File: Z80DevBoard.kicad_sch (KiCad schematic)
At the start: 170 parts, among them J1 Conn_01x02_Pin, J2 Conn_02x20_Top_Bottom, J3 Conn_02x10_Top_Bottom, SW1 WAIT, SW2 RESET, SW3 Z80BOOT, SW4 RPBOOT, SW5 SW_Nidec_CAS-120A1, SW6 Z80_CLOCK, U1 74HC14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

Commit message: Fixed the size of the footprint of the fuse.
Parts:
- F1: footprint Fuse:Fuse_0402_1005Metric -> Fuse:Fuse_0603_1608Metric
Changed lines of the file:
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@@
 	(title_block
 		(title "Z80DevBoard")
-		(date "2026-03-26")
+		(date "2026-03-30")
 		(company "Gianluca Rainis")
 		(comment 1 "gianluca-rainis on GitHub")
@@
 			)
 		)
-		(property "Footprint" "Fuse:Fuse_0402_1005Metric"
+		(property "Footprint" "Fuse:Fuse_0603_1608Metric"
 			(at 22.098 40.64 90)
 			(effects

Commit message: Made a custom footprint for the switch.
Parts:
- SW5: footprint Button_Switch_THT:SW_Slide_SPDT_Straight_CK_OS102011MS2Q -> customFootprints:SW_Slide-03_Wuerth-WS-SLTV
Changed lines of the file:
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@@
 			)
 		)
-		(property "Footprint" "Button_Switch_THT:SW_Slide_SPDT_Straight_CK_OS102011MS2Q"
+		(property "Footprint" "customFootprints:SW_Slide-03_Wuerth-WS-SLTV"
 			(at 128.27 55.88 0)
 			(effects

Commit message: Fixed the size of the capacitors.
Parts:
- C1, C10, C11, C12, C13, C14, C2, C3, C4, C5, C6, C7, C8, C9: footprint Capacitor_THT:CP_Radial_D4.0mm_P2.00mm -> Capacitor_THT:CP_Radial_D5.0mm_P2.50mm
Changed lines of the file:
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@@
 	(title_block
 		(title "Z80DevBoard")
-		(date "2026-03-30")
+		(date "2026-03-31")
 		(company "Gianluca Rainis")
 		(comment 1 "gianluca-rainis on GitHub")
@@
 			)
 		)
-		(property "Footprint" "Capacitor_THT:CP_Radial_D4.0mm_P2.00mm"
+		(property "Footprint" "Capacitor_THT:CP_Radial_D5.0mm_P2.50mm"
 			(at 221.2848 287.02 0)
 			(effects
@@
 			)
 		)
-		(property "Footprint" "Capacitor_THT:CP_Radial_D4.0mm_P2.00mm"
+		(property "Footprint" "Capacitor_THT:CP_Radial_D5.0mm_P2.50mm"
 			(at 110.7948 25.4 0)
 			(effects
@@
 			)
 		)
-		(property "Footprint" "Capacitor_THT:CP_Radial_D4.0mm_P2.00mm"
+		(property "Footprint" "Capacitor_THT:CP_Radial_D5.0mm_P2.50mm"
 			(at 20.6248 72.39 0)
 			(effects
@@
 			)
 		)
-		(property "Footprint" "Capacitor_THT:CP_Radial_D4.0mm_P2.00mm"
+		(property "Footprint" "Capacitor_THT:CP_Radial_D5.0mm_P2.50mm"
 			(at 43.4848 31.75 0)
 			(effects
@@
 			)
 		)
-		(property "Footprint" "Capacitor_THT:CP_Radial_D4.0mm_P2.00mm"
+		(property "Footprint" "Capacitor_THT:CP_Radial_D5.0mm_P2.50mm"
 			(at 80.3148 261.62 0)
 			(effects
@@
 			)
 		)
-		(property "Footprint" "Capacitor_THT:CP_Radial_D4.0mm_P2.00mm"
+		(property "Footprint" "Capacitor_THT:CP_Radial_D5.0mm_P2.50mm"
 			(at 71.4248 72.39 0)
 			(effects
@@
 			)
 		)
-		(property "Footprint" "Capacitor_THT:CP_Radial_D4.0mm_P2.00mm"
+		(property "Footprint" "Capacitor_THT:CP_Radial_D5.0mm_P2.50mm"
 			(at 66.3448 31.75 0)
 			(effects
@@
 			)
 		)
-		(property "Footprint" "Capacitor_THT:CP_Radial_D4.0mm_P2.00mm"
+		(property "Footprint" "Capacitor_THT:CP_Radial_D5.0mm_P2.50mm"
 			(at 218.7448 322.58 0)
 			(effects
@@
 			)
 		)
-		(property "Footprint" "Capacitor_THT:CP_Radial_D4.0mm_P2.00mm"
+		(property "Footprint" "Capacitor_THT:CP_Radial_D5.0mm_P2.50mm"
 			(at 91.7448 64.77 0)
 			(effects
@@
 			)
 		)
-		(property "Footprint" "Capacitor_THT:CP_Radial_D4.0mm_P2.00mm"
+		(property "Footprint" "Capacitor_THT:CP_Radial_D5.0mm_P2.50mm"
 			(at 221.2848 252.73 0)
 			(effects
@@
 			)
 		)
-		(property "Footprint" "Capacitor_THT:CP_Radial_D4.0mm_P2.00mm"
+		(property "Footprint" "Capacitor_THT:CP_Radial_D5.0mm_P2.50mm"
 			(at 32.0548 72.39 0)
 			(effects
@@
 			)
 		)
-		(property "Footprint" "Capacitor_THT:CP_Radial_D4.0mm_P2.00mm"
+		(property "Footprint" "Capacitor_THT:CP_Radial_D5.0mm_P2.50mm"
 			(at 44.7548 72.39 0)
 			(effects
@@
 			)
 		)
-		(property "Footprint" "Capacitor_THT:CP_Radial_D4.0mm_P2.00mm"
+		(property "Footprint" "Capacitor_THT:CP_Radial_D5.0mm_P2.50mm"
 			(at 57.4548 72.39 0)
 			(effects
@@
 			)
 		)
-		(property "Footprint" "Capacitor_THT:CP_Radial_D4.0mm_P2.00mm"
+		(property "Footprint" "Capacitor_THT:CP_Radial_D5.0mm_P2.50mm"
 			(at 120.9548 25.4 0)
 			(effects

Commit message: Fixed the switch button.
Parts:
- F1: footprint Fuse:Fuse_0603_1608Metric -> Fuse:Fuse_0805_2012Metric
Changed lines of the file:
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@@
 			)
 		)
-		(property "Footprint" "Fuse:Fuse_0603_1608Metric"
+		(property "Footprint" "Fuse:Fuse_0805_2012Metric"
 			(at 22.098 40.64 90)
 			(effects

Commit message: Fixed the capacitor's footprint.
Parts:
- C1, C10, C11, C12, C13, C14, C2, C3, C4, C5, C6, C7, C8, C9: footprint Capacitor_THT:CP_Radial_D5.0mm_P2.50mm -> Capacitor_THT:CP_Radial_Tantal_D5.0mm_P5.00mm
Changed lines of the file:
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@@
 			)
 		)
-		(property "Footprint" "Capacitor_THT:CP_Radial_D5.0mm_P2.50mm"
+		(property "Footprint" "Capacitor_THT:CP_Radial_Tantal_D5.0mm_P5.00mm"
 			(at 221.2848 287.02 0)
 			(effects
@@
 			)
 		)
-		(property "Footprint" "Capacitor_THT:CP_Radial_D5.0mm_P2.50mm"
+		(property "Footprint" "Capacitor_THT:CP_Radial_Tantal_D5.0mm_P5.00mm"
 			(at 110.7948 25.4 0)
 			(effects
@@
 			)
 		)
-		(property "Footprint" "Capacitor_THT:CP_Radial_D5.0mm_P2.50mm"
+		(property "Footprint" "Capacitor_THT:CP_Radial_Tantal_D5.0mm_P5.00mm"
 			(at 20.6248 72.39 0)
 			(effects
@@
 			)
 		)
-		(property "Footprint" "Capacitor_THT:CP_Radial_D5.0mm_P2.50mm"
+		(property "Footprint" "Capacitor_THT:CP_Radial_Tantal_D5.0mm_P5.00mm"
 			(at 43.4848 31.75 0)
 			(effects
@@
 			)
 		)
-		(property "Footprint" "Capacitor_THT:CP_Radial_D5.0mm_P2.50mm"
+		(property "Footprint" "Capacitor_THT:CP_Radial_Tantal_D5.0mm_P5.00mm"
 			(at 80.3148 261.62 0)
 			(effects
@@
 			)
 		)
-		(property "Footprint" "Capacitor_THT:CP_Radial_D5.0mm_P2.50mm"
+		(property "Footprint" "Capacitor_THT:CP_Radial_Tantal_D5.0mm_P5.00mm"
 			(at 71.4248 72.39 0)
 			(effects
@@
 			)
 		)
-		(property "Footprint" "Capacitor_THT:CP_Radial_D5.0mm_P2.50mm"
+		(property "Footprint" "Capacitor_THT:CP_Radial_Tantal_D5.0mm_P5.00mm"
 			(at 66.3448 31.75 0)
 			(effects
@@
 			)
 		)
-		(property "Footprint" "Capacitor_THT:CP_Radial_D5.0mm_P2.50mm"
+		(property "Footprint" "Capacitor_THT:CP_Radial_Tantal_D5.0mm_P5.00mm"
 			(at 218.7448 322.58 0)
 			(effects
@@
 			)
 		)
-		(property "Footprint" "Capacitor_THT:CP_Radial_D5.0mm_P2.50mm"
+		(property "Footprint" "Capacitor_THT:CP_Radial_Tantal_D5.0mm_P5.00mm"
 			(at 91.7448 64.77 0)
 			(effects
@@
 			)
 		)
-		(property "Footprint" "Capacitor_THT:CP_Radial_D5.0mm_P2.50mm"
+		(property "Footprint" "Capacitor_THT:CP_Radial_Tantal_D5.0mm_P5.00mm"
 			(at 221.2848 252.73 0)
 			(effects
@@
 			)
 		)
-		(property "Footprint" "Capacitor_THT:CP_Radial_D5.0mm_P2.50mm"
+		(property "Footprint" "Capacitor_THT:CP_Radial_Tantal_D5.0mm_P5.00mm"
 			(at 32.0548 72.39 0)
 			(effects
@@
 			)
 		)
-		(property "Footprint" "Capacitor_THT:CP_Radial_D5.0mm_P2.50mm"
+		(property "Footprint" "Capacitor_THT:CP_Radial_Tantal_D5.0mm_P5.00mm"
 			(at 44.7548 72.39 0)
 			(effects
@@
 			)
 		)
-		(property "Footprint" "Capacitor_THT:CP_Radial_D5.0mm_P2.50mm"
+		(property "Footprint" "Capacitor_THT:CP_Radial_Tantal_D5.0mm_P5.00mm"
 			(at 57.4548 72.39 0)
 			(effects
@@
 			)
 		)
-		(property "Footprint" "Capacitor_THT:CP_Radial_D5.0mm_P2.50mm"
+		(property "Footprint" "Capacitor_THT:CP_Radial_Tantal_D5.0mm_P5.00mm"
 			(at 120.9548 25.4 0)
 			(effects

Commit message: Fixed some footprints and connections.
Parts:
- F1: footprint Fuse:Fuse_0805_2012Metric -> Fuse:Fuse_1206_3216Metric
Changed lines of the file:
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@@
 			)
 		)
-		(property "Footprint" "Fuse:Fuse_0805_2012Metric"
+		(property "Footprint" "Fuse:Fuse_1206_3216Metric"
 			(at 22.098 40.64 90)
 			(effects

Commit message: Updated the USB-C footprint. Continued the BOM.
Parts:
- USB_C1: footprint Connector_USB:USB_C_Receptacle_GCT_USB4085 -> Connector_USB:USB_C_Receptacle_HRO_TYPE-C-31-M-12
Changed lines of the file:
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@@
 			)
 		)
-		(property "Footprint" "Connector_USB:USB_C_Receptacle_GCT_USB4085"
+		(property "Footprint" "Connector_USB:USB_C_Receptacle_HRO_TYPE-C-31-M-12"
 			(at 528.32 344.17 0)
 			(effects

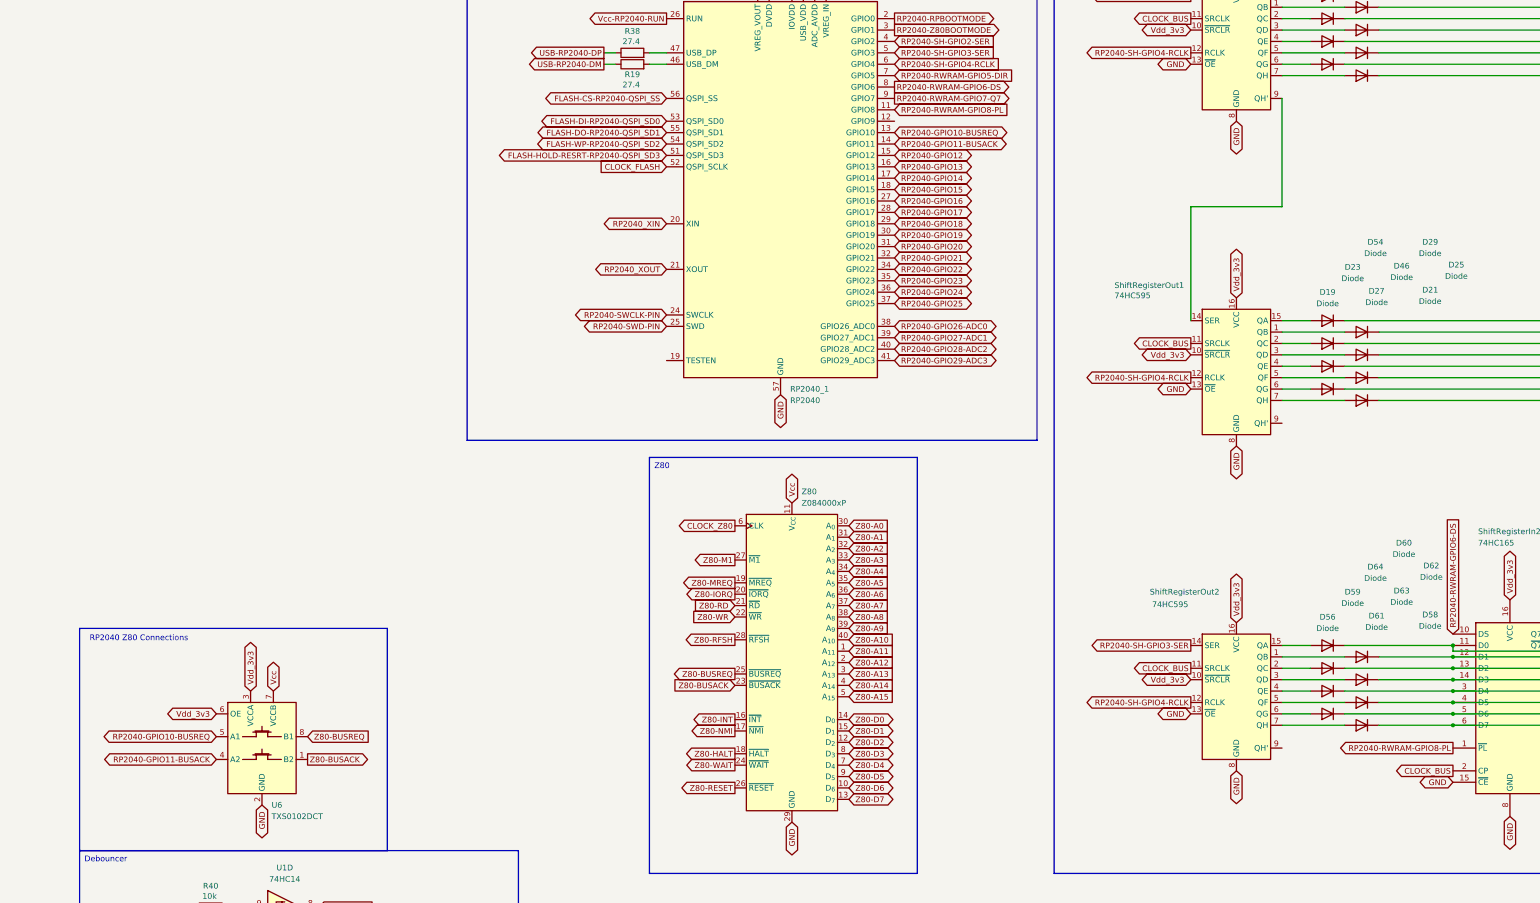
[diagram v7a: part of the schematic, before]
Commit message: Started working on the firmware. Replaced the TXS0102DCT with an TXS0104EPW to handle the Z80 RESET. Updated the BOM.
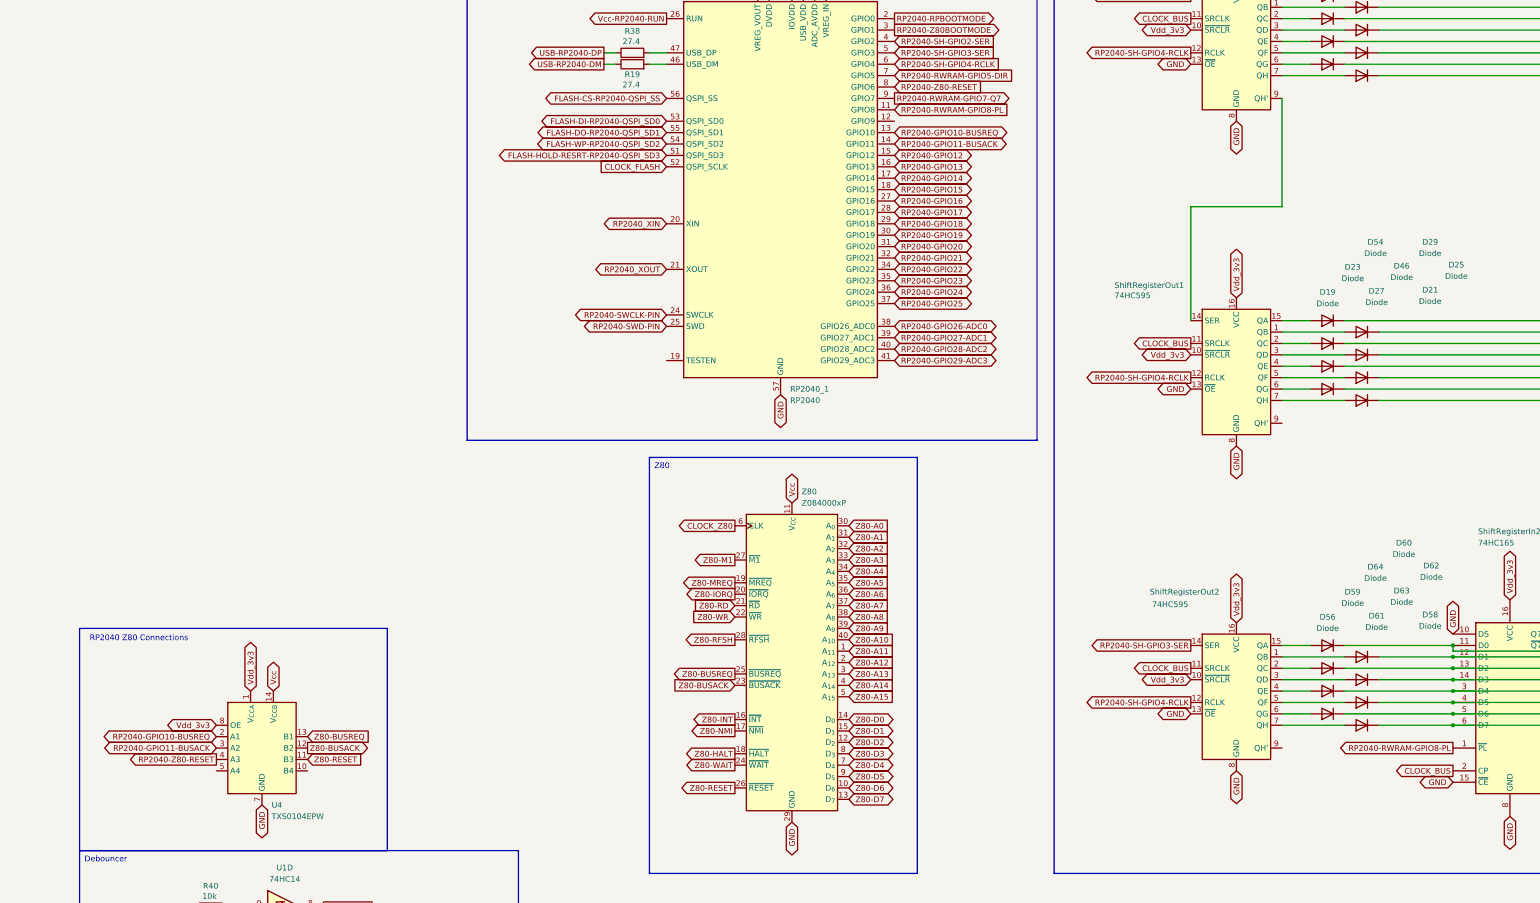
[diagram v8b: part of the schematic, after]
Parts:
- removed U6: TXS0102DCT, Package_SO:SSOP-8_2.95x2.8mm_P0.65mm, symbol Logic_LevelTranslator:TXS0102DCT
- added U4: TXS0104EPW, Package_SO:TSSOP-14_4.4x5mm_P0.65mm, symbol Logic_LevelTranslator:TXS0104EPW
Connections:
- net GND: now also ShiftRegisterIn2.10 (DS), U4.7 (GND)
- net RP2040-GPIO10-BUSREQ: now also U4.2 (A1)
- net RP2040-GPIO11-BUSACK: now also U4.3 (A2)
- net Vcc: now also U4.14 (V_{CCB})
- net Vdd_3v3: now also U4.1 (V_{CCA}), U4.8 (OE)
- net Z80-BUSACK: now also U4.12 (B2)
- net Z80-BUSREQ: now also U4.13 (B1)
- net Z80-RESET: now also U4.11 (B3)
- net RP2040-RWRAM-GPIO6-DS renamed RP2040-Z80-RESET
- net RP2040-Z80-RESET: now also U4.4 (A3); no longer ShiftRegisterIn2.10 (DS)
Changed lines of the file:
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@@
 		)
 	)
+	(global_label "GND"
+		(shape bidirectional)
+		(at 490.22 185.42 90)
+		(fields_autoplaced yes)
+		(effects
+			(font
+				(size 1.27 1.27)
+			)
+			(justify left)
+		)
+		(property "Intersheetrefs" "${INTERSHEET_REFS}"
+			(at 490.22 177.453 90)
+			(effects
+				(font
+					(size 1.27 1.27)
+				)
+				(justify left)
+				(hide yes)
+			)
+		)
+	)
 	(global_label "RAM-A9"
 		(shape output)
@@
 		)
 	)
-	(global_label "RP2040-RWRAM-GPIO6-DS"
-		(shape output)
+	(global_label "RP2040-Z80-RESET"
+		(shape input)
 		(at 365.76 63.5 0)
 		(fields_autoplaced yes)
@@
 		)
 		(property "Intersheetrefs" "${INTERSHEET_REFS}"
-			(at 395.5361 63.5 0)
+			(at 388.6416 63.5 0)
 			(effects
 				(font
@@
 		)
 	)
-	(global_label "RP2040-RWRAM-GPIO6-DS"
-		(shape input)
-		(at 490.22 185.42 90)
-		(fields_autoplaced yes)
-		(effects
-			(font
-				(size 1.27 1.27)
-			)
-			(justify left)
-		)
-		(property "Intersheetrefs" "${INTERSHEET_REFS}"
-			(at 490.22 155.6439 90)
-			(effects
-				(font
-					(size 1.27 1.27)
-				)
-				(justify left)
-				(hide yes)
-			)
-		)
-	)
 	(global_label "Vcc"
 		(shape bidirectional)
@@
 		)
 	)
+	(global_label "Z80-RESET"
+		(shape input)
+		(at 234.95 213.36 0)
+		(fields_autoplaced yes)
+		(effects
+			(font
+				(size 1.27 1.27)
+			)
+			(justify left)
+		)
+		(property "Intersheetrefs" "${INTERSHEET_REFS}"
+			(at 248.8812 213.36 0)
+			(effects
+				(font
+					(size 1.27 1.27)
+				)
+				(justify left)
+				(hide yes)
+			)
+		)
+	)
 	(global_label "Z80-NMI"
 		(shape input)
@@
 		)
 	)
-	(global_label "RP2040-GPIO11-BUSACK"
-		(shape bidirectional)
-		(at 214.63 213.36 180)
-		(fields_autoplaced yes)
-		(effects
-			(font
-				(size 1.27 1.27)
-			)
-			(justify right)
-		)
-		(property "Intersheetrefs" "${INTERSHEET_REFS}"
-			(at 185.6778 213.36 0)
-			(effects
-				(font
-					(size 1.27 1.27)
-				)
-				(justify right)
-				(hide yes)
-			)
-		)
-	)
 	(global_label "RAM-Q4"
 		(shape bidirectional)
@@
 		)
 	)
+	(global_label "RP2040-GPIO11-BUSACK"
+		(shape bidirectional)
+		(at 214.63 210.82 180)
+		(fields_autoplaced yes)
+		(effects
+			(font
+				(size 1.27 1.27)
+			)
+			(justify right)
+		)
+		(property "Intersheetrefs" "${INTERSHEET_REFS}"
+			(at 185.6778 210.82 0)
+			(effects
+				(font
+					(size 1.27 1.27)
+				)
+				(justify right)
+				(hide yes)
+			)
+		)
+	)
 	(global_label "GND"
 		(shape bidirectional)
@@
 	(global_label "Vdd_3v3"
 		(shape bidirectional)
-		(at 214.63 203.2 180)
+		(at 214.63 205.74 180)
 		(fields_autoplaced yes)
 		(effects
@@
 		)
 		(property "Intersheetrefs" "${INTERSHEET_REFS}"
-			(at 202.7927 203.2 0)
+			(at 202.7927 205.74 0)
 			(effects
 				(font
@@
 		)
 	)
+	(global_label "RP2040-Z80-RESET"
+		(shape output)
+		(at 214.63 213.36 180)
+		(fields_autoplaced yes)
+		(effects
+			(font
+				(size 1.27 1.27)
+			)
+			(justify right)
+		)
+		(property "Intersheetrefs" "${INTERSHEET_REFS}"
+			(at 191.7484 213.36 0)
+			(effects
+				(font
+					(size 1.27 1.27)
+				)
+				(justify right)
+				(hide yes)
+			)
+		)
+	)
 	(global_label "RAM-A2"
 		(shape output)
@@
 		)
 	)
+	(global_label "Z80-BUSACK"
+		(shape output)
+		(at 234.95 210.82 0)
+		(fields_autoplaced yes)
+		(effects
+			(font
+				(size 1.27 1.27)
+			)
+			(justify left)
+		)
+		(property "Intersheetrefs" "${INTERSHEET_REFS}"
+			(at 250.5747 210.82 0)
+			(effects
+				(font
+					(size 1.27 1.27)
+				)
+				(justify left)
+				(hide yes)
+			)
+		)
+	)
 	(global_label "RAM-A0"
 		(shape output)
@@
 		)
 	)
-	(global_label "Z80-BUSACK"
-		(shape output)
-		(at 234.95 213.36 0)
-		(fields_autoplaced yes)
-		(effects
-			(font
-				(size 1.27 1.27)
-			)
-			(justify left)
-		)
-		(property "Intersheetrefs" "${INTERSHEET_REFS}"
-			(at 250.5747 213.36 0)
-			(effects
-				(font
-					(size 1.27 1.27)
-				)
-				(justify left)
-				(hide yes)
-			)
-		)
-	)
 	(global_label "GND"
 		(shape bidirectional)
@@
 	)
 	(symbol
-		(lib_id "Logic_LevelTranslator:TXS0102DCT")
-		(at 224.79 210.82 0)
-		(unit 1)
-		(exclude_from_sim no)
-		(in_bom yes)
-		(on_board yes)
-		(dnp no)
-		(fields_autoplaced yes)
-		(property "Reference" "U6"
-			(at 226.9333 223.52 0)
-			(effects
-				(font
-					(size 1.27 1.27)
-				)
-				(justify left)
-			)
-		)
-		(property "Value" "TXS0102DCT"
-			(at 226.9333 226.06 0)
-			(effects
-				(font
-					(size 1.27 1.27)
-				)
-				(justify left)
-			)
-		)
-		(property "Footprint" "Package_SO:SSOP-8_2.95x2.8mm_P0.65mm"
-			(at 224.79 224.79 0)
-			(effects
-				(font
-					(size 1.27 1.27)
-				)
-				(hide yes)
-			)
-		)
-		(property "Datasheet" "http://www.ti.com/lit/gpn/txs0102"
-			(at 224.79 211.328 0)
-			(effects
-				(font
-					(size 1.27 1.27)
-				)
-				(hide yes)
-			)
-		)
-		(property "Description" "2-Bit Bidirectional Voltage-Level Shifter for Open-Drain and Push-Pull Application, SSOP-8"
-			(at 224.79 210.82 0)
-			(effects
-				(font
-					(size 1.27 1.27)
-				)
-				(hide yes)
-			)
-		)
-		(pin "8"
-		)
-		(pin "6"
-		)
-		(pin "5"
-		)
-		(pin "2"
-		)
-		(pin "4"
-		)
-		(pin "3"
-		)
-		(pin "7"
-		)
-		(pin "1"
-		)
-		(instances
-			(project ""
-				(path "/e1d3a7c4-9081-48b0-8f4d-5da429793ec4"
-					(reference "U6")
-					(unit 1)
-				)
-			)
-		)
-	)
-	(symbol
 		(lib_id "Diode:1N4148WT")
 		(at 469.9 190.5 180)
@@
 				)
 			)
+		)
+	)
+	(symbol
+		(lib_id "Logic_LevelTranslator:TXS0104EPW")
+		(at 224.79 210.82 0)
+		(unit 1)
+		(exclude_from_sim no)
+		(in_bom yes)
+		(on_board yes)
+		(dnp no)
+		(fields_autoplaced yes)
+		(property "Reference" "U4"
+			(at 226.9333 223.52 0)
+			(effects
+				(font
+					(size 1.27 1.27)
+				)
+				(justify left)
+			)
+		)
+		(property "Value" "TXS0104EPW"
+			(at 226.9333 226.06 0)
+			(effects
+				(font
+					(size 1.27 1.27)
+				)
+				(justify left)
+			)
+		)
+		(property "Footprint" "Package_SO:TSSOP-14_4.4x5mm_P0.65mm"
+			(at 226.06 222.25 0)
+			(effects
+				(font
+					(size 1.27 1.27)
+				)
+				(justify left)
+				(hide yes)
+			)
+		)
+		(property "Datasheet" "www.ti.com/lit/ds/symlink/txs0104e.pdf"
+			(at 226.06 224.79 0)
+			(effects
+				(font
+					(size 1.27 1.27)
+				)
+				(justify left)
+				(hide yes)
+			)
+		)
+		(property "Description" "Bidirectional  level-shifting voltage translator, TSSOP-14"
+			(at 226.06 227.33 0)
+			(effects
+				(font
+					(size 1.27 1.27)
+				)
+				(justify left)
+				(hide yes)
+			)
+		)
+		(pin "9"
+		)
+		(pin "5"
+		)
+		(pin "2"
+		)
+		(pin "6"
+		)
+		(pin "14"
+		)
+		(pin "11"
+		)
+		(pin "3"
+		)
+		(pin "12"
+		)
+		(pin "10"
+		)
+		(pin "1"
+		)
+		(pin "7"
+		)
+		(pin "8"
+		)
+		(pin "13"
+		)
+		(pin "4"
+		)
+		(instances
+			(project ""
+				(path "/e1d3a7c4-9081-48b0-8f4d-5da429793ec4"
+					(reference "U4")
+					(unit 1)
+				)
+			)
